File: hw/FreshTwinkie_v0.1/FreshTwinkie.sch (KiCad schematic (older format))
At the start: 50 parts, among them J1 USB_C_Receptacle, J2 USB_B_Micro, P1 USB_C_Plug, Q1 BSD840NH6327XTSA1, Q2 BSD840NH6327XTSA1, Q3 BSD840NH6327XTSA1, Q4 BSD840NH6327XTSA1, SW1 SW_Push, U1 AD8606ARMZ-REEL, U2 STM32F072CBUx, U3 AP2112K, U4 INA260, U5 INA260

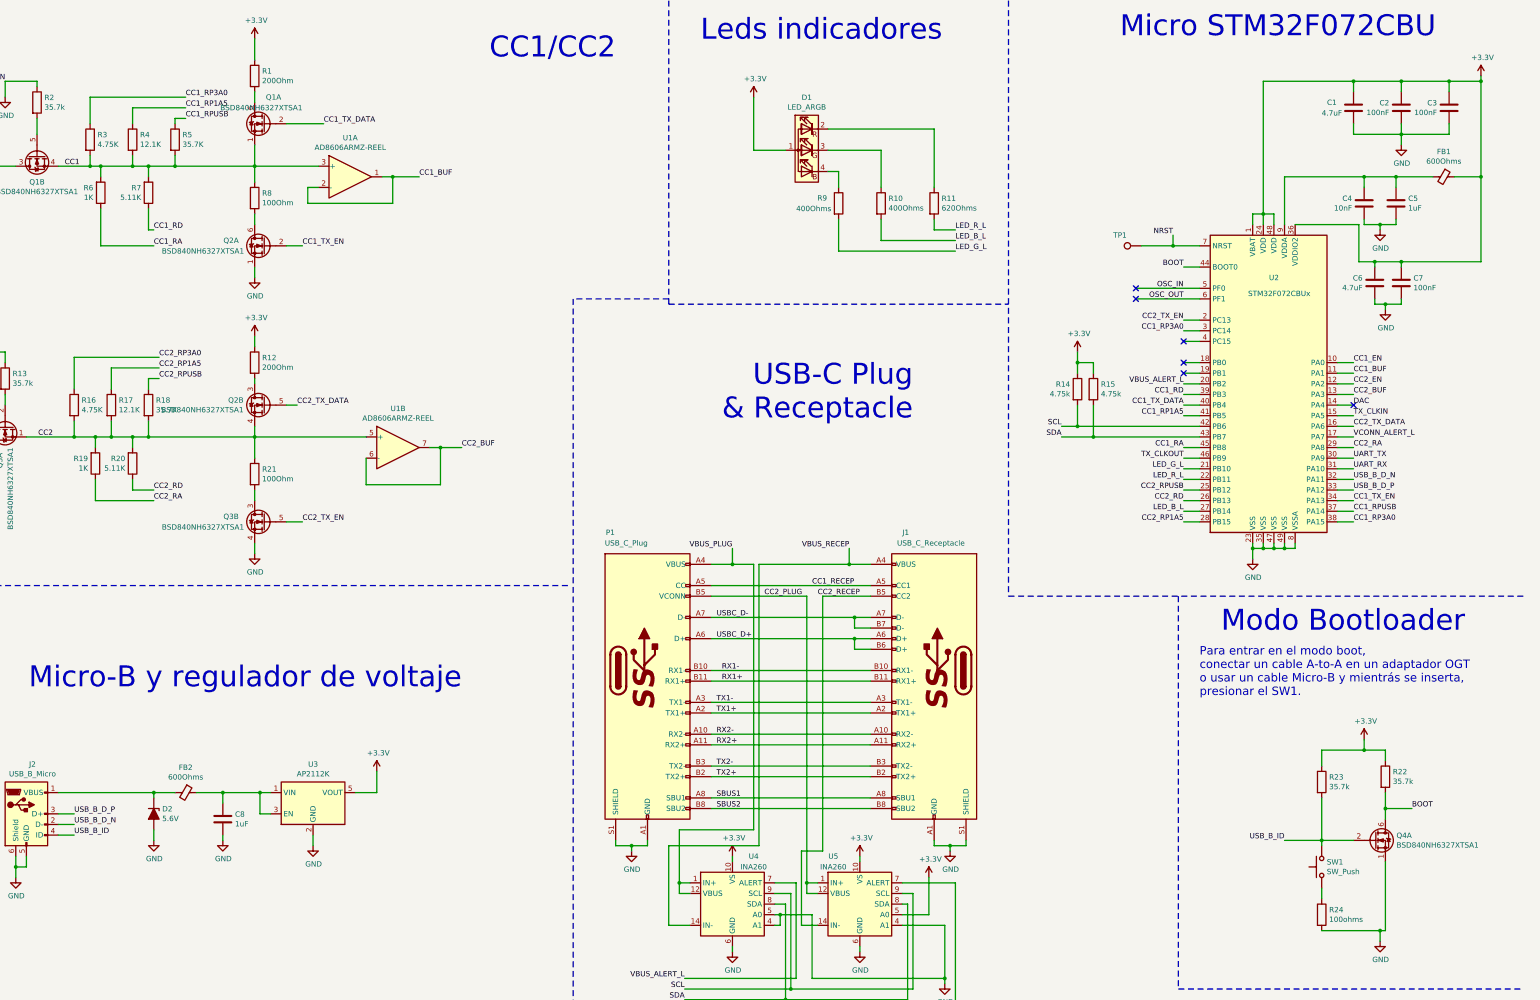
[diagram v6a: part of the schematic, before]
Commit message: addfootprints&PN
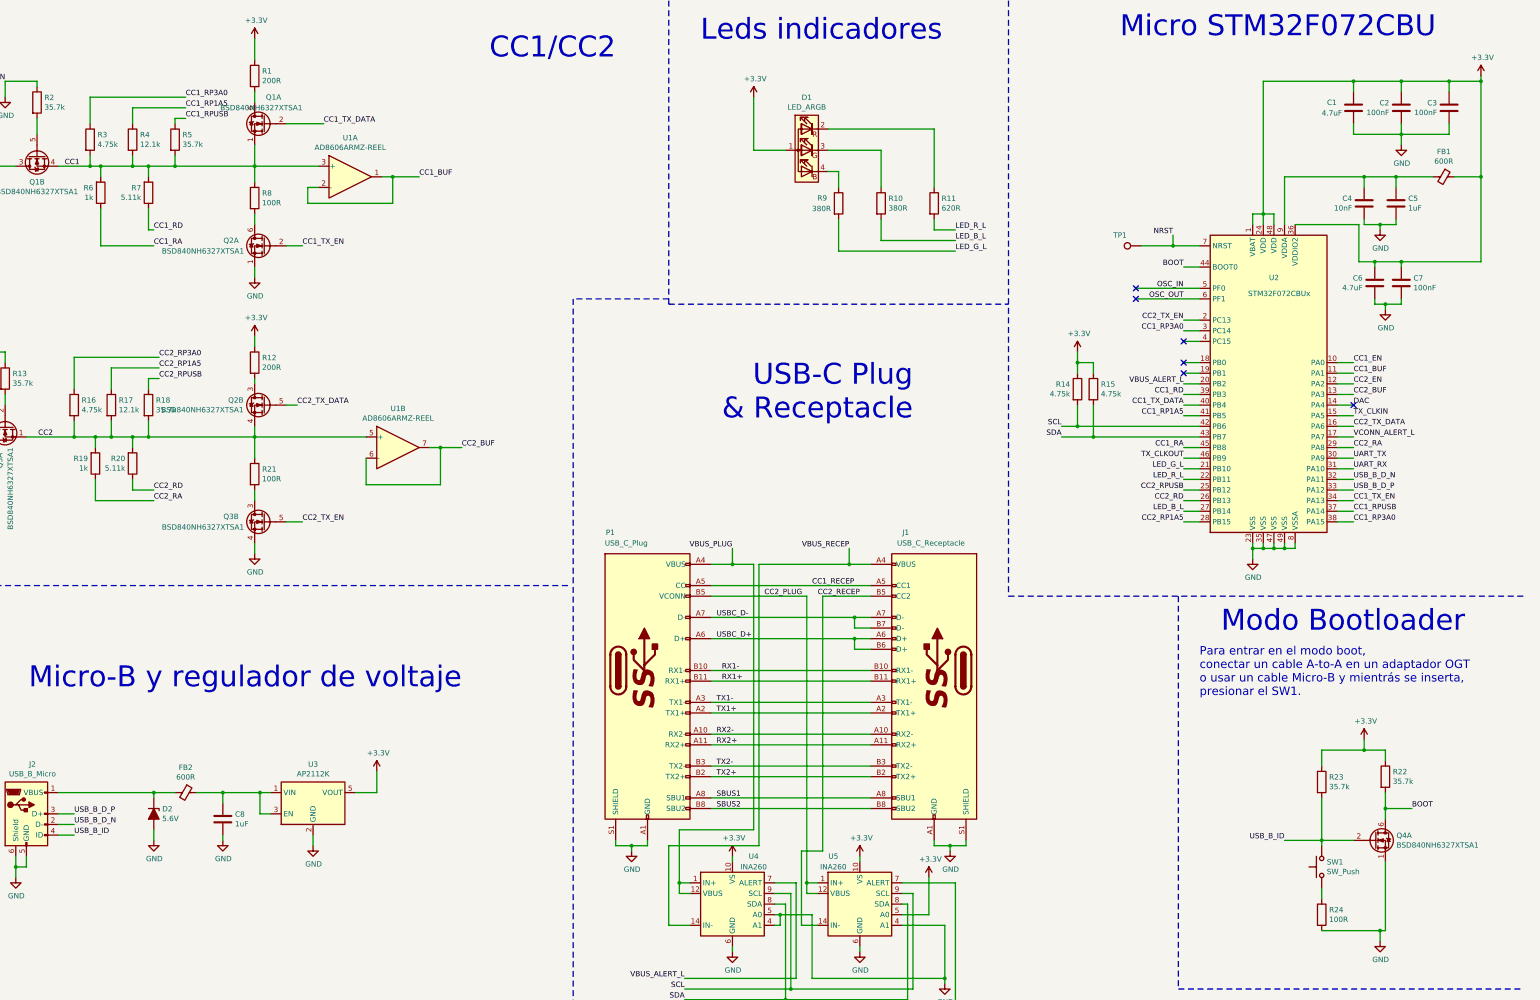
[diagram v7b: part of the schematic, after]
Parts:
- C1, C6: footprint (none) -> Capacitor_SMD:C_0805_2012Metric; Mfg (none) -> Taiyo Yuden; PN (none) -> C385902; Tienda (none) -> LCSC
- C2, C3, C7: footprint (none) -> Capacitor_SMD:C_0805_2012Metric; Mfg (none) -> Samsung; PN (none) -> 187-CL21F104ZAANNNC; Tienda (none) -> Mouser
- C4: footprint (none) -> Capacitor_SMD:C_0805_2012Metric; Mfg (none) -> YAGEO; PN (none) -> C83170; Tienda (none) -> LCSC
- C5, C8: footprint (none) -> Capacitor_SMD:C_0805_2012Metric; Mfg (none) -> Samsung; PN (none) -> 187-CL21B105KOFNFNE; Tienda (none) -> Mouser
- D1: footprint (none) -> LED_SMD:LED_Cree-PLCC4_3.2x2.8mm_CCW; Mfg (none) -> Cree, Inc.; PN (none) -> 941-VBAFKACAEDH8B7A3; Tienda (none) -> Mouser
- D2: footprint (none) -> Diode_SMD:D_SOD-123; Mfg (none) -> Diodes Incorporated; PN (none) -> 621-BZT52C5V6-13-F; Tienda (none) -> Mouser
- FB1, FB2: value 600Ohms -> 600R; footprint (none) -> Inductor_SMD:L_0805_2012Metric_Pad1.15x1.40mm_HandSolder; Mfg (none) -> Murata Electronics; PN (none) -> 81-BLM21A601F; Tienda (none) -> Mouser
- J1: footprint (none) -> Connectors:C393939; Mfg (none) -> SHOU HAN; PN (none) -> C393939; Tienda (none) -> LCSC
- J2: footprint (none) -> Connectors:U254051N4BH806; Mfg (none) -> XKB Connectivity; PN (none) -> C319170; Tienda (none) -> LCSC
- R1, R12: value 200Ohm -> 200R; footprint (none) -> Resistor_SMD:R_0805_2012Metric; Mfg (none) -> PANASONIC; PN (none) -> C473273; Tienda (none) -> LCSC
- R10, R9: value 400Ohms -> 380R; footprint (none) -> Resistor_SMD:R_0805_2012Metric; Mfg (none) -> BOURNS; PN (none) -> 652-CR0805FX-3830ELF; Tienda (none) -> Mouser
- R11: value 620Ohms -> 620R; footprint (none) -> Resistor_SMD:R_0805_2012Metric; Mfg (none) -> YAGEO; PN (none) -> 603-RC0402FR-07620RL; Tienda (none) -> Mouser
- R13, R2, R22, R23: footprint (none) -> Resistor_SMD:R_0805_2012Metric; Mfg (none) -> Viking Tech; PN (none) -> C218528; Tienda (none) -> LCSC
- R14, R15: footprint (none) -> Resistor_SMD:R_0805_2012Metric; Mfg (none) -> UNI-ROYAL; PN (none) -> C425496; Tienda (none) -> LCSC
- R16, R3: value 4.75K -> 4.75k; footprint (none) -> Resistor_SMD:R_0805_2012Metric; Mfg (none) -> UNI-ROYAL; PN (none) -> C425496; Tienda (none) -> LCSC
- R17, R4: value 12.1K -> 12.1k; footprint (none) -> Resistor_SMD:R_0805_2012Metric; Mfg (none) -> Viking Tech; PN (none) -> C217800; Tienda (none) -> LCSC
- R18, R5: value 35.7K -> 35.7k; footprint (none) -> Resistor_SMD:R_0805_2012Metric; Mfg (none) -> Viking Tech; PN (none) -> C218528; Tienda (none) -> LCSC
- R19, R6: value 1K -> 1k; footprint (none) -> Resistor_SMD:R_0805_2012Metric; Mfg (none) -> FH; PN (none) -> C115302; Tienda (none) -> LCSC
- R20, R7: value 5.11K -> 5.11k; footprint (none) -> Resistor_SMD:R_0805_2012Metric; Mfg (none) -> BOURNS; PN (none) -> C204553; Tienda (none) -> LCSC
- R21, R8: value 100Ohm -> 100R; footprint (none) -> Resistor_SMD:R_0805_2012Metric; Mfg (none) -> Viking Tech; PN (none) -> C515718; Tienda (none) -> LCSC
- R24: value 100ohms -> 100R; footprint (none) -> Resistor_SMD:R_0805_2012Metric; Mfg (none) -> Viking Tech; PN (none) -> C515718; Tienda (none) -> LCSC
- TP1: footprint (none) -> TestPoint:TestPoint_Pad_D1.5mm
- U1: footprint (none) -> Package_SO:MSOP-8_3x3mm_P0.65mm; PN C459905 -> C459905
- U1: footprint (none) -> Package_SO:MSOP-8_3x3mm_P0.65mm
- U2: Mfg STMicroelectronics -> STMicro; PN STM32F042C6T6TR -> 511-STM32F042C6T6TR
- U3: PN AP2112K-3.3TRG1 -> 621-AP2112K-3.3TRG1
- U4, U5: footprint Package_SO:TSSOP-16_4.4x5mm_P0.65mm -> (none)

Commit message: allcomponentsready&boom
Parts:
- P1: footprint (none) -> DX07P024MJ1R1500(1):JAE_DX07P024MJ1R1500; Mfg (none) -> JAE; PN (none) -> 656-DX07P024MJ1500; Tienda (none) -> Mouser
- SW1: footprint (none) -> Connectors:C455281; Mfg (none) -> XUNPU; PN (none) -> C455281; Tienda (none) -> LCSC
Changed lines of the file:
@@
 F 0 "P1" H 7450 8200 50  0000 C CNN
 F 1 "USB_C_Plug" H 7600 8100 50  0000 C CNN
-F 2 "" H 7950 6900 50  0001 C CNN
-F 3 "" H 7950 6900 50  0001 C CNN
-F 4 "" H 7800 6900 50  0001 C CNN "Mfg"
-F 5 "" H 7800 6900 50  0001 C CNN "PN"
+F 2 "DX07P024MJ1R1500(1):JAE_DX07P024MJ1R1500" H 7950 6900 50  0001 C CNN
+F 3 "https://www.jae.com/direct/topics/topics_file_download/topics_id=66505&ext_no=06&index=0&_lang=en&v=2019122712575883906509" H 7950 6900 50  0001 C CNN
+F 4 "JAE" H 7800 6900 50  0001 C CNN "Mfg"
+F 5 "656-DX07P024MJ1500" H 7800 6900 50  0001 C CNN "PN"
+F 6 "Mouser" H 7800 6900 50  0001 C CNN "Tienda"
 	1    7800 6900
 	1    0    0    -1
@@
 F 0 "SW1" V 14196 8702 50  0000 R CNN
 F 1 "SW_Push" V 14105 8702 50  0000 R CNN
-F 2 "" H 14150 8950 50  0001 C CNN
-F 3 "~" H 14150 8950 50  0001 C CNN
+F 2 "Connectors:C455281" H 14150 8950 50  0001 C CNN
+F 3 "https://datasheet.lcsc.com/szlcsc/1912111437_XUNPU-TS-1088R-02526_C455281.pdf" H 14150 8950 50  0001 C CNN
+F 4 "XUNPU" H 14150 8750 50  0001 C CNN "Mfg"
+F 5 "C455281" H 14150 8750 50  0001 C CNN "PN"
+F 6 "LCSC" H 14150 8750 50  0001 C CNN "Tienda"
 	1    14150 8750
 	0    -1   -1   0
